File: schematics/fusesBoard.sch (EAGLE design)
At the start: 25 parts, among them Q1 IRF540, Q2 IRF540, Q3 IRF540

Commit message: разведена плата для пережигателей
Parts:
- removed JP10, JP11: (no value), pinhead:PINHD-1X1
- added JP13, JP14, JP15: (no value), pinhead:PINHD-1X1
- R1: value (none) -> 10k; device rcl:R-US_0207/12 -> resistor:R-US_0204/7
- R2, R7, R8: device rcl:R-US_0207/12 -> resistor:R-US_0204/7
- R3: value (none) -> 1k; device rcl:R-US_0207/12 -> resistor:R-US_0204/7
- R4: value 1k -> (none); device rcl:R-US_0207/12 -> resistor:R-US_0204/7
- R5: value 10k -> 1k; device rcl:R-US_0207/12 -> resistor:R-US_0204/7
- R6: value 1k -> 10k; device rcl:R-US_0207/12 -> resistor:R-US_0204/7
- R9: value 10k -> (none); device rcl:R-US_0207/12 -> resistor:R-US_0204/7
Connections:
- removed net +7V: JP4.1, JP7.1, JP9.1, R4.2, R6.2, R8.1
- new net VCC1: JP13.1, JP7.1, R8.2
- new net VCC2: JP14.1, JP4.1, R3.2
- new net VCC3: JP15.1, JP9.1, R5.2
- net GND: now also R4.1, R6.1; no longer R3.2, R5.1
- net N$10: now also R1.2; no longer R5.2
- net N$11: now also R3.1; no longer R4.1
- net N$15: now also R8.1; no longer R6.1
- net N$18: now also R9.2; no longer R1.2
- net N$20: now also R6.2; no longer R9.2
- net N$22: now also R5.1; no longer R8.2
- net N$26: now also R4.2; no longer R3.1
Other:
- moved on the sheet: JP5, JP6, JP7, R1, R3, R4, R5, R6, R8, R9

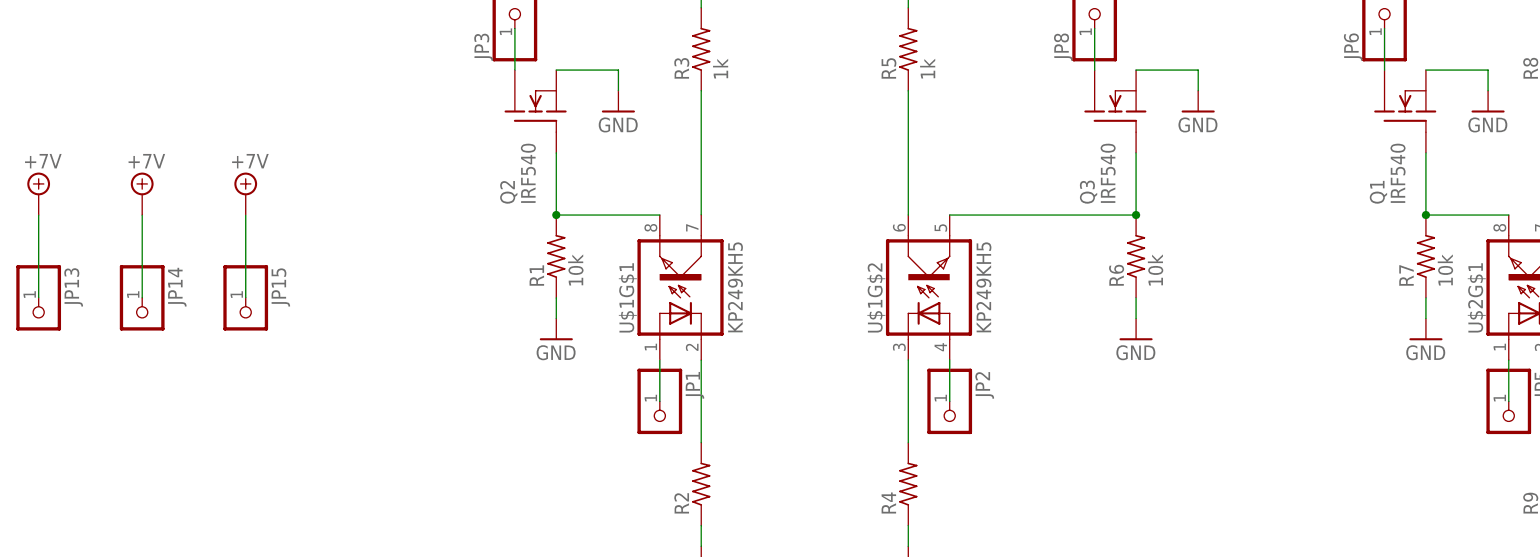
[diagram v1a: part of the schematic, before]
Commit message: сделаны площадки под пережигатели, увеличена ширина дорожек
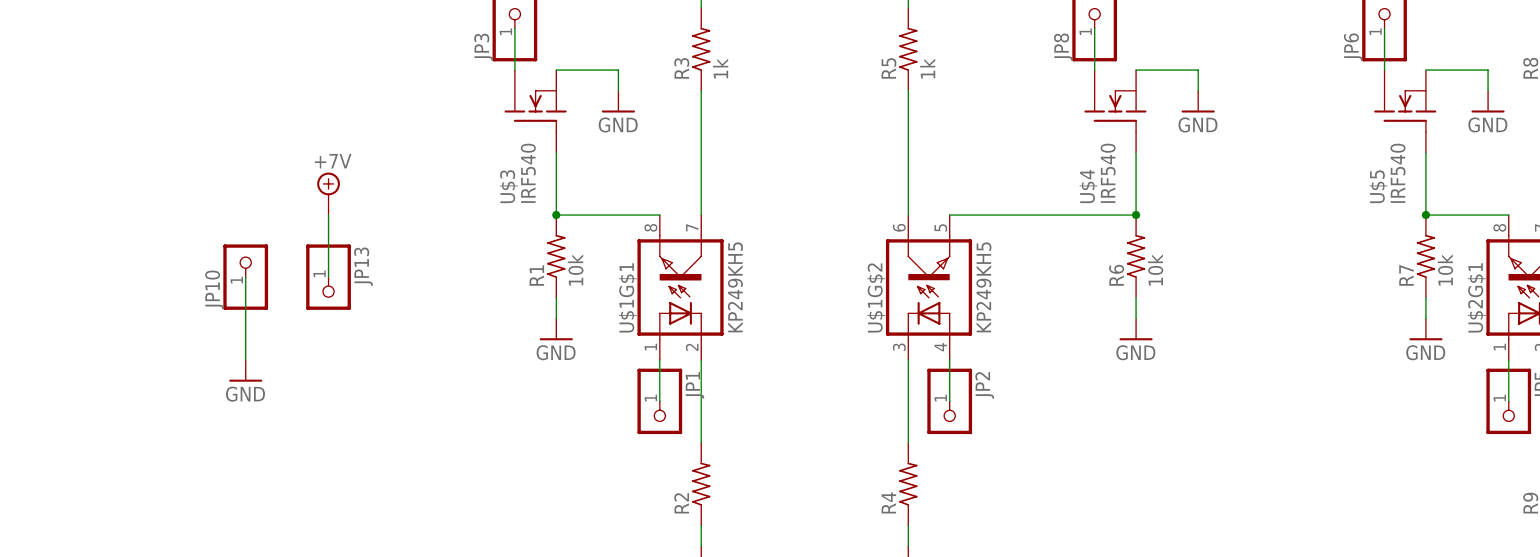
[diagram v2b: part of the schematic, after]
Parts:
- removed JP14, JP15: (no value), pinhead:PINHD-1X1
- removed Q1, Q2, Q3: IRF540, transistor-fet:IRF540
- added JP10: (no value), pinhead:PINHD-1X1
- added U$3, U$4, U$5: IRF540, optron1:IRF540
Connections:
- removed net VCC1: JP13.1, JP7.1, R8.2
- removed net VCC2: JP14.1, JP4.1, R3.2
- removed net VCC3: JP15.1, JP9.1, R5.2
- new net VCC: JP13.1, JP4.1, JP7.1, JP9.1, R3.2, R5.2, R8.2
- net GND: now also JP10.1, U$3.SOURCE, U$4.SOURCE, U$5.SOURCE; no longer Q1.S, Q2.S, Q3.S
- net N$1: now also U$5.DRAIN; no longer Q1.D
- net N$10: now also U$3.GATE; no longer Q2.G
- net N$12: now also U$5.GATE; no longer Q1.G
- net N$14: now also U$3.DRAIN; no longer Q2.D
- net N$20: now also U$4.GATE; no longer Q3.G
- net N$23: now also U$4.DRAIN; no longer Q3.D
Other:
- moved on the sheet: JP13

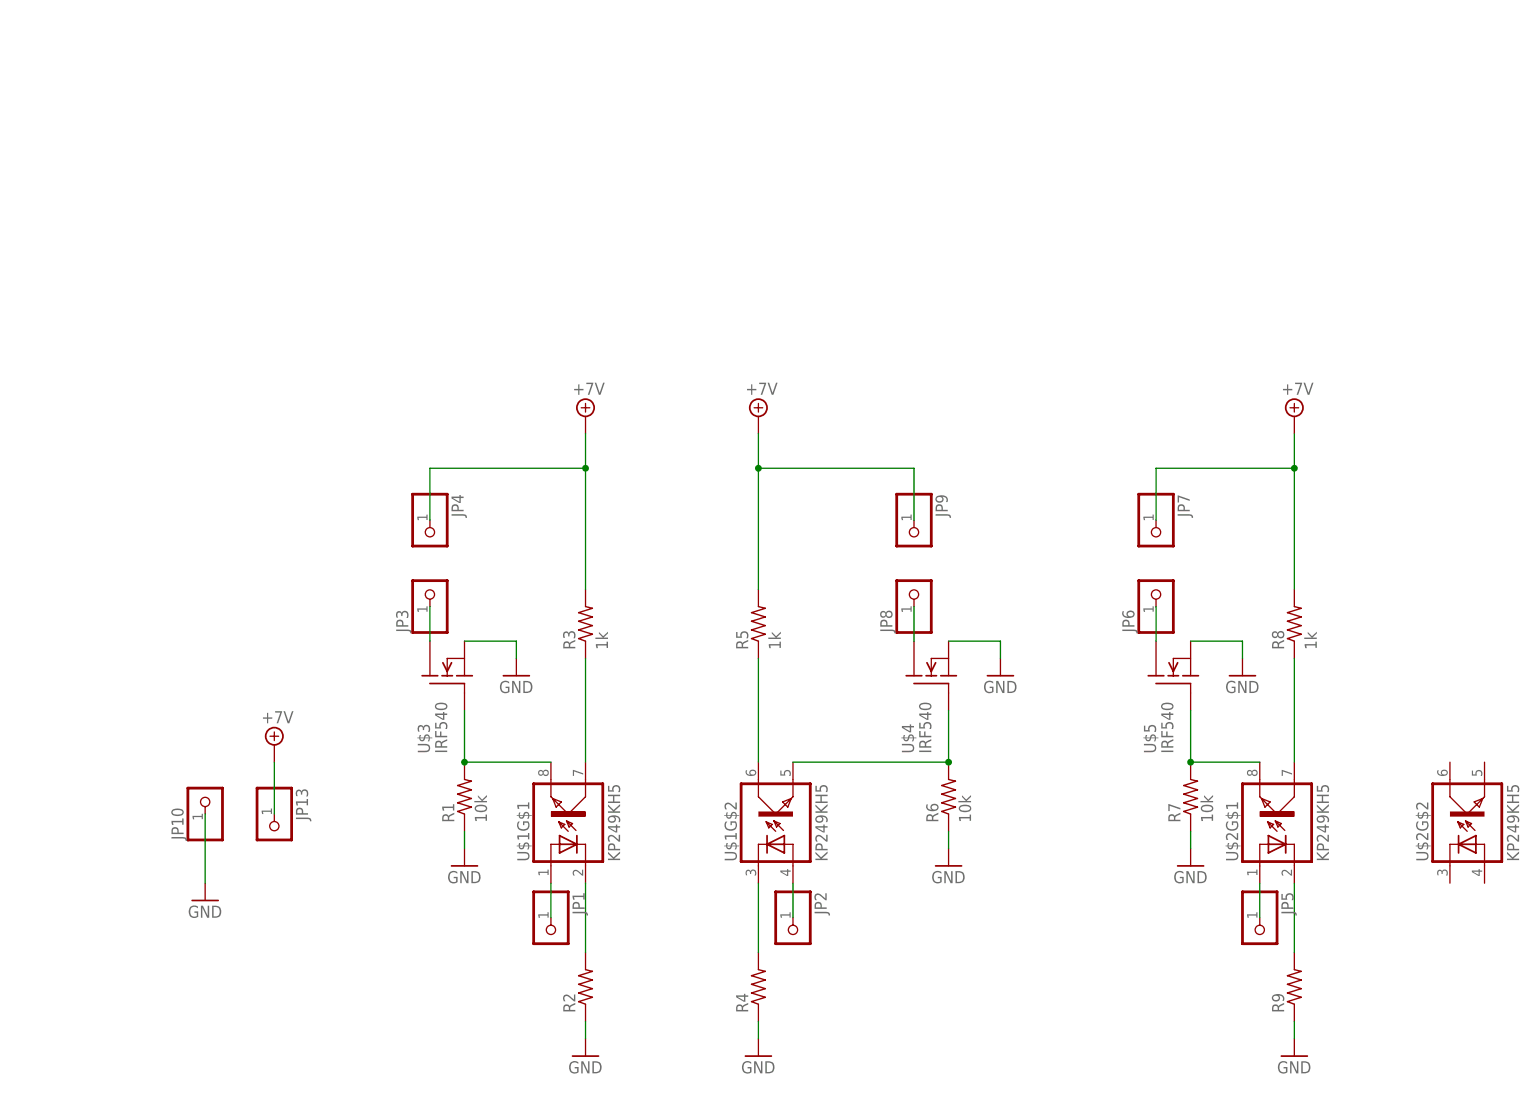
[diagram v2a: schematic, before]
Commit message: переразведенная схема платы
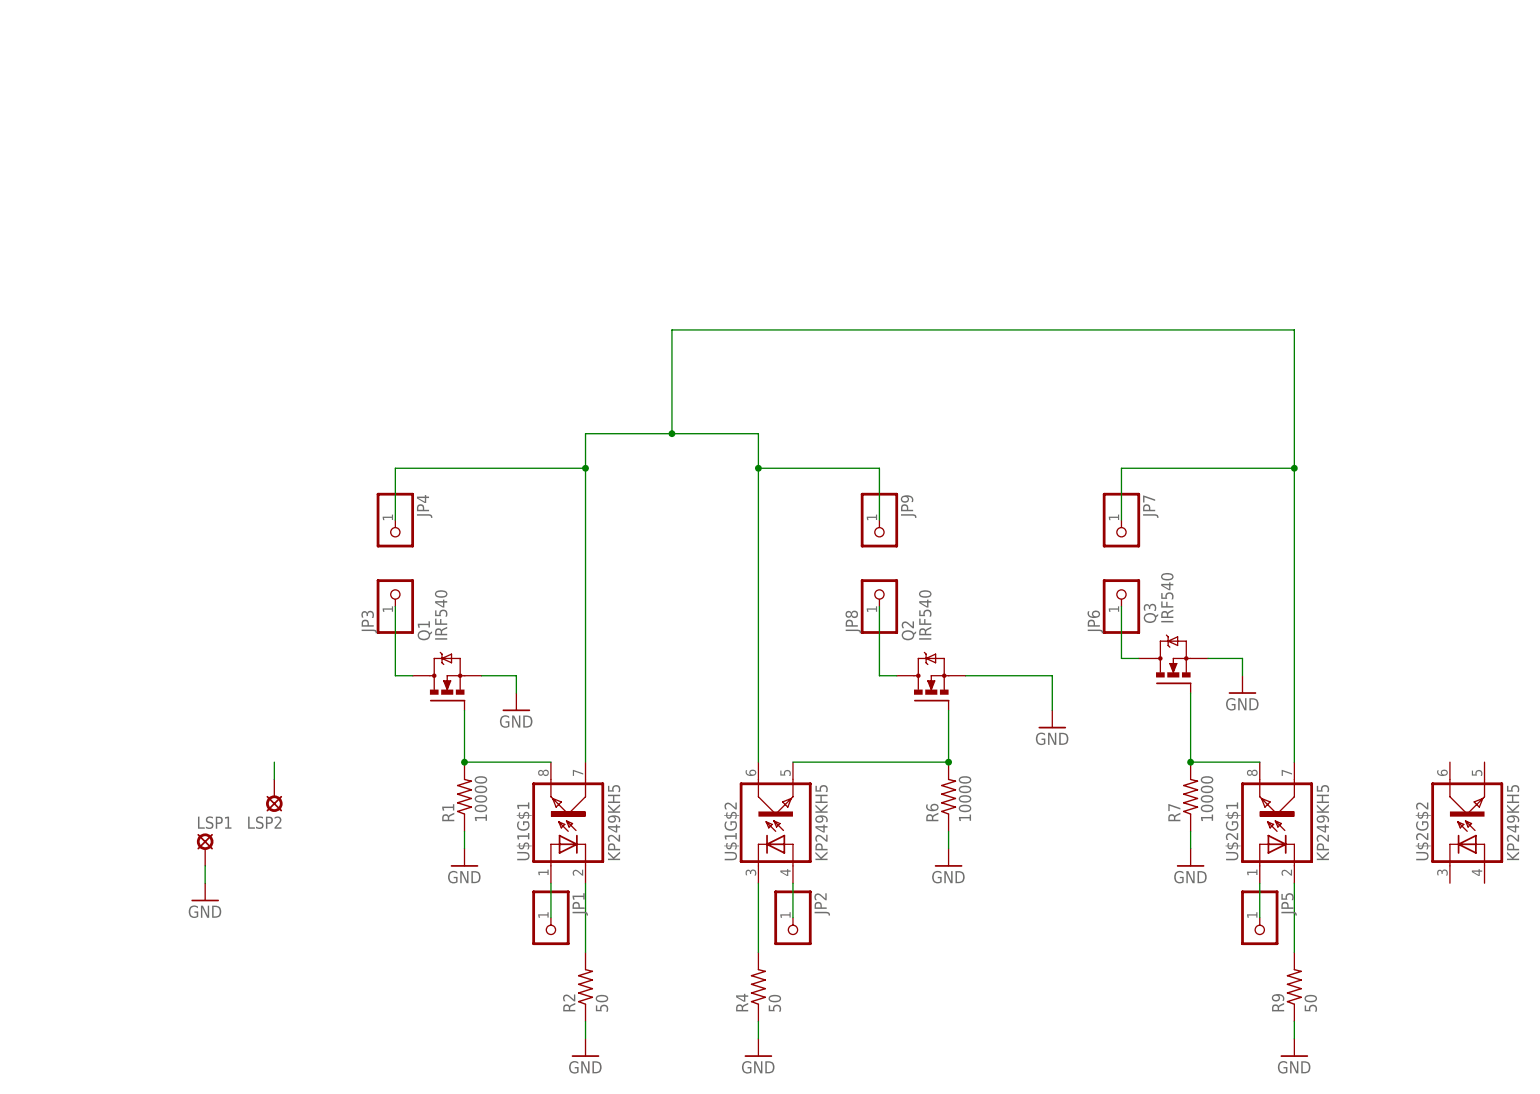
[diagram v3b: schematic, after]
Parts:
- removed JP10, JP13: (no value), pinhead:PINHD-1X1
- removed R3, R5, R8: 1k, resistor:R-US_0204/7
- removed U$3, U$4, U$5: IRF540, optron1:IRF540
- added LSP1, LSP2: SE14, solpad:SE14
- added Q1, Q2, Q3: IRF540, transistor-power:IRF540
- R1, R6, R7: value 10k -> 10000
- R2, R4, R9: value (none) -> 50
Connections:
- net N$13 renamed CTRL1
- net N$2 renamed CTRL3
- net N$25 renamed CTRL2
- removed net N$1: JP6.1, U$5.DRAIN
- removed net N$10: R1.2, U$1G$1.8, U$3.GATE
- removed net N$11: R3.1, U$1G$1.7
- removed net N$12: R7.2, U$2G$1.8, U$5.GATE
- removed net N$14: JP3.1, U$3.DRAIN
- removed net N$15: R8.1, U$2G$1.7
- removed net N$20: R6.2, U$1G$2.5, U$4.GATE
- removed net N$22: R5.1, U$1G$2.6
- removed net N$23: JP8.1, U$4.DRAIN
- new net GATE1: Q1.G, R1.2, U$1G$1.8
- new net GATE2: Q2.G, R6.2, U$1G$2.5
- new net GATE3: Q3.G, R7.2, U$2G$1.8
- new net SOURCE1: JP3.1, Q1.D
- new net SOURCE2: JP8.1, Q2.D
- new net SOURCE3: JP6.1, Q3.D
- net GND: now also LSP1.MP, Q1.S, Q2.S, Q3.S; no longer JP10.1, U$3.SOURCE, U$4.SOURCE, U$5.SOURCE
- net VCC: now also LSP2.MP, U$1G$1.7, U$1G$2.6, U$2G$1.7; no longer JP13.1, R3.2, R5.2, R8.2
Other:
- moved on the sheet: JP3, JP4, JP6, JP7, JP8, JP9

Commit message: made on earth
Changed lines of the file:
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@@
 <pinref part="GND10" gate="1" pin="GND"/>
 <wire x1="-129.54" y1="-195.58" x2="-129.54" y2="-198.12" width="0.1524" layer="91"/>
+<label x="-137.16" y="-195.58" size="1.778" layer="95"/>
 </segment>
 </net>
@@
 <wire x1="-73.66" y1="-132.08" x2="-60.96" y2="-132.08" width="0.1524" layer="91"/>
 <junction x="-60.96" y="-132.08"/>
+<label x="-66.04" y="-116.84" size="1.778" layer="95"/>
 </segment>
 <segment>
 <pinref part="LSP2" gate="1" pin="MP"/>
 <wire x1="-119.38" y1="-182.88" x2="-119.38" y2="-180.34" width="0.1524" layer="91"/>
+<label x="-124.46" y="-180.34" size="1.778" layer="95"/>
 </segment>
 </net>
@@
 </sheet>
 </sheets>
+<errors>
+</errors>
 </schematic>
 </drawing>
